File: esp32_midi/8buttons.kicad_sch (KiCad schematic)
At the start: 14 parts, among them SW2 SW_SPST, SW3 SW_SPST, SW4 SW_SPST, SW5 SW_SPST, SW6 SW_SPST, SW7 SW_SPST, SW8 SW_SPST, SW9 SW_SPST, U6 USBLC6-4SC6

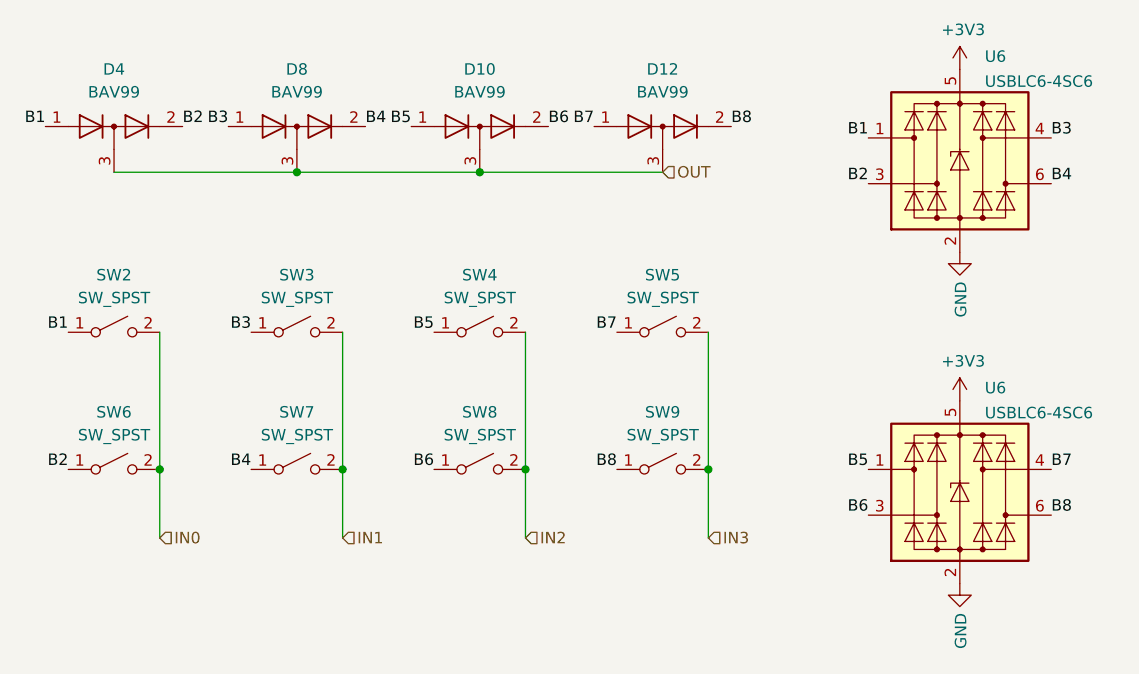
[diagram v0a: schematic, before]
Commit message: More footprints applied
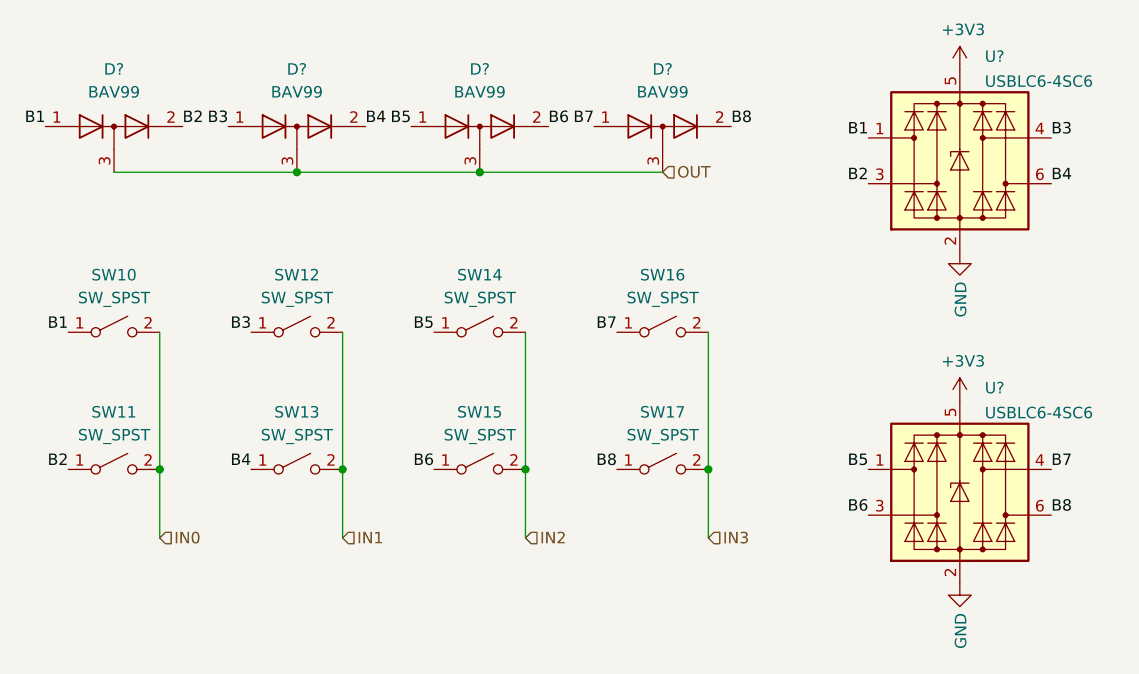
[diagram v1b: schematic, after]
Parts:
- renumbered D10 to D?, D4 to D?, D12 to D?, D8 to D?, SW2 to SW10, SW6 to SW11, SW3 to SW12, SW7 to SW13, SW4 to SW14, SW8 to SW15, SW5 to SW16, SW9 to SW17, U6 to U?
